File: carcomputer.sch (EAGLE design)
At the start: 23 parts, among them K1 351, Q1 BUZ10, Q2 BUZ10, T1 2N2219, X1 B3B-ZR

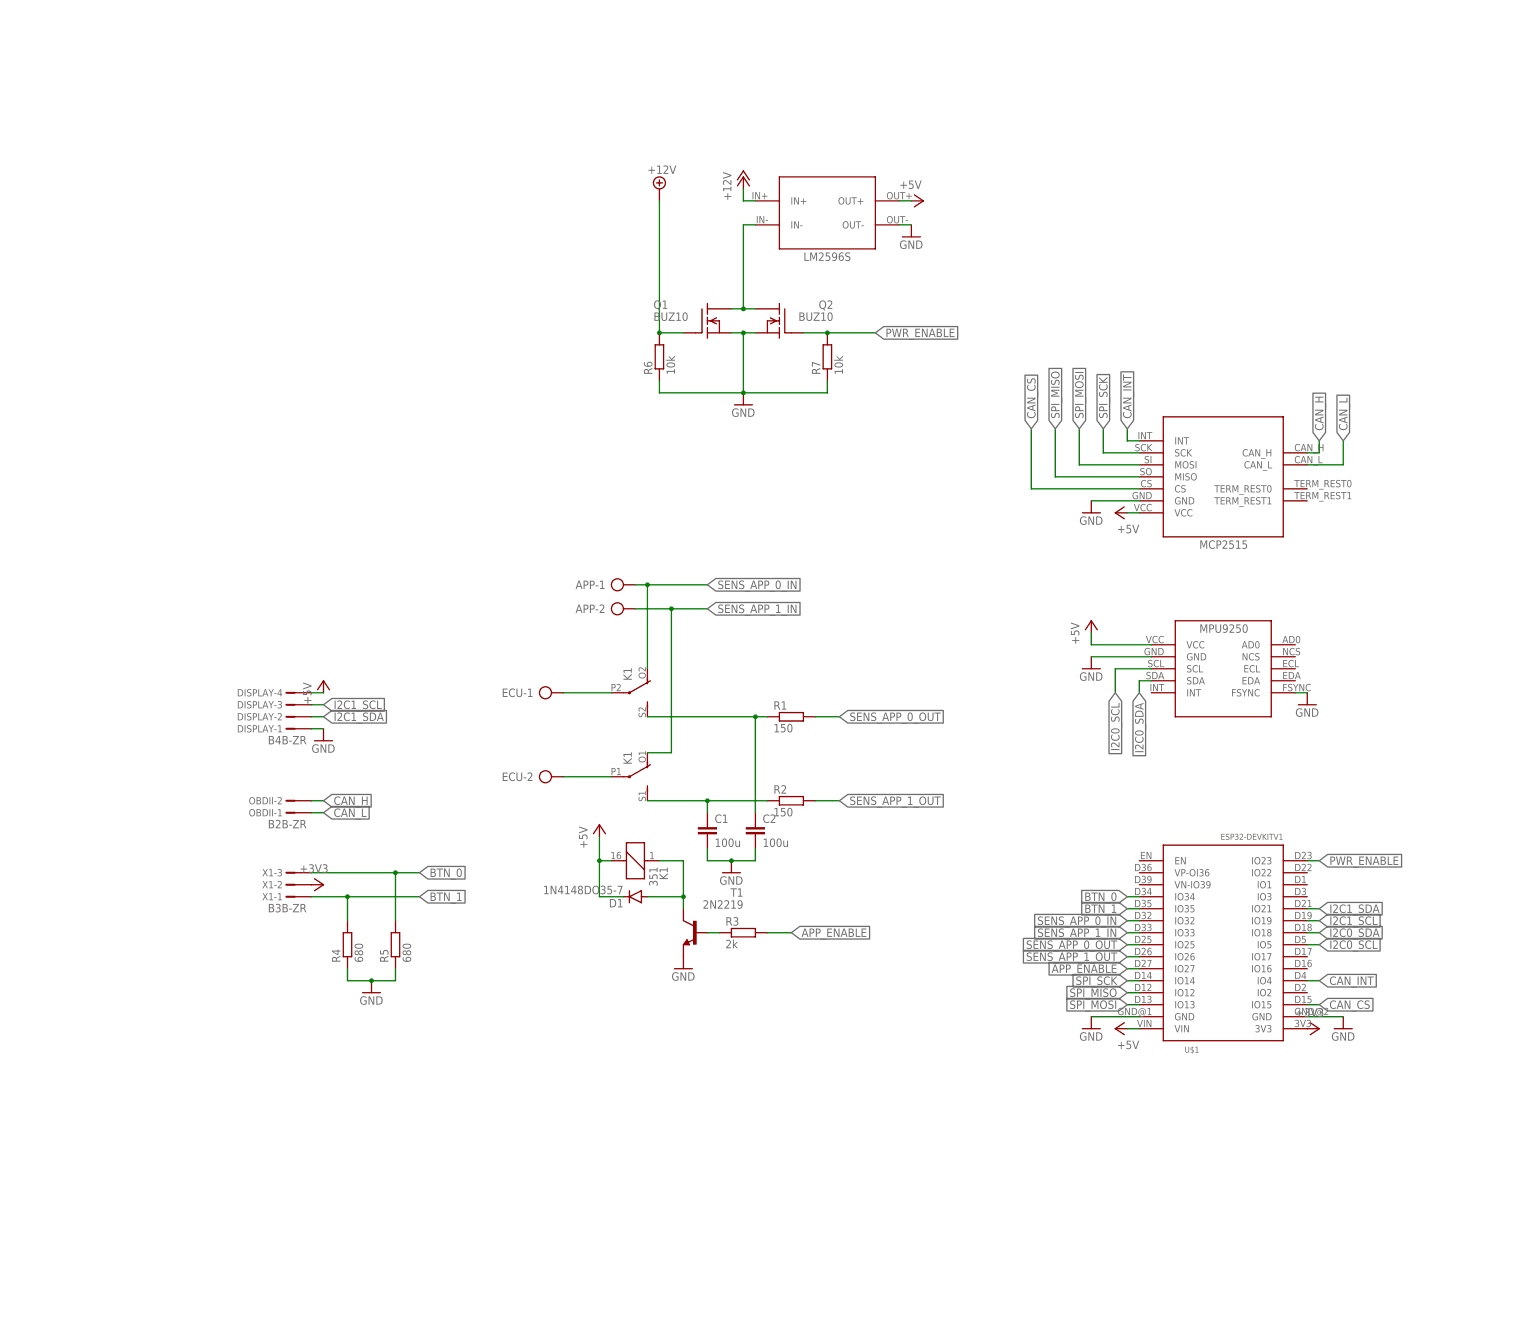
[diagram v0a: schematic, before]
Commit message: Added alternative power circuit. Added connection jumpers. Remapped some pins.
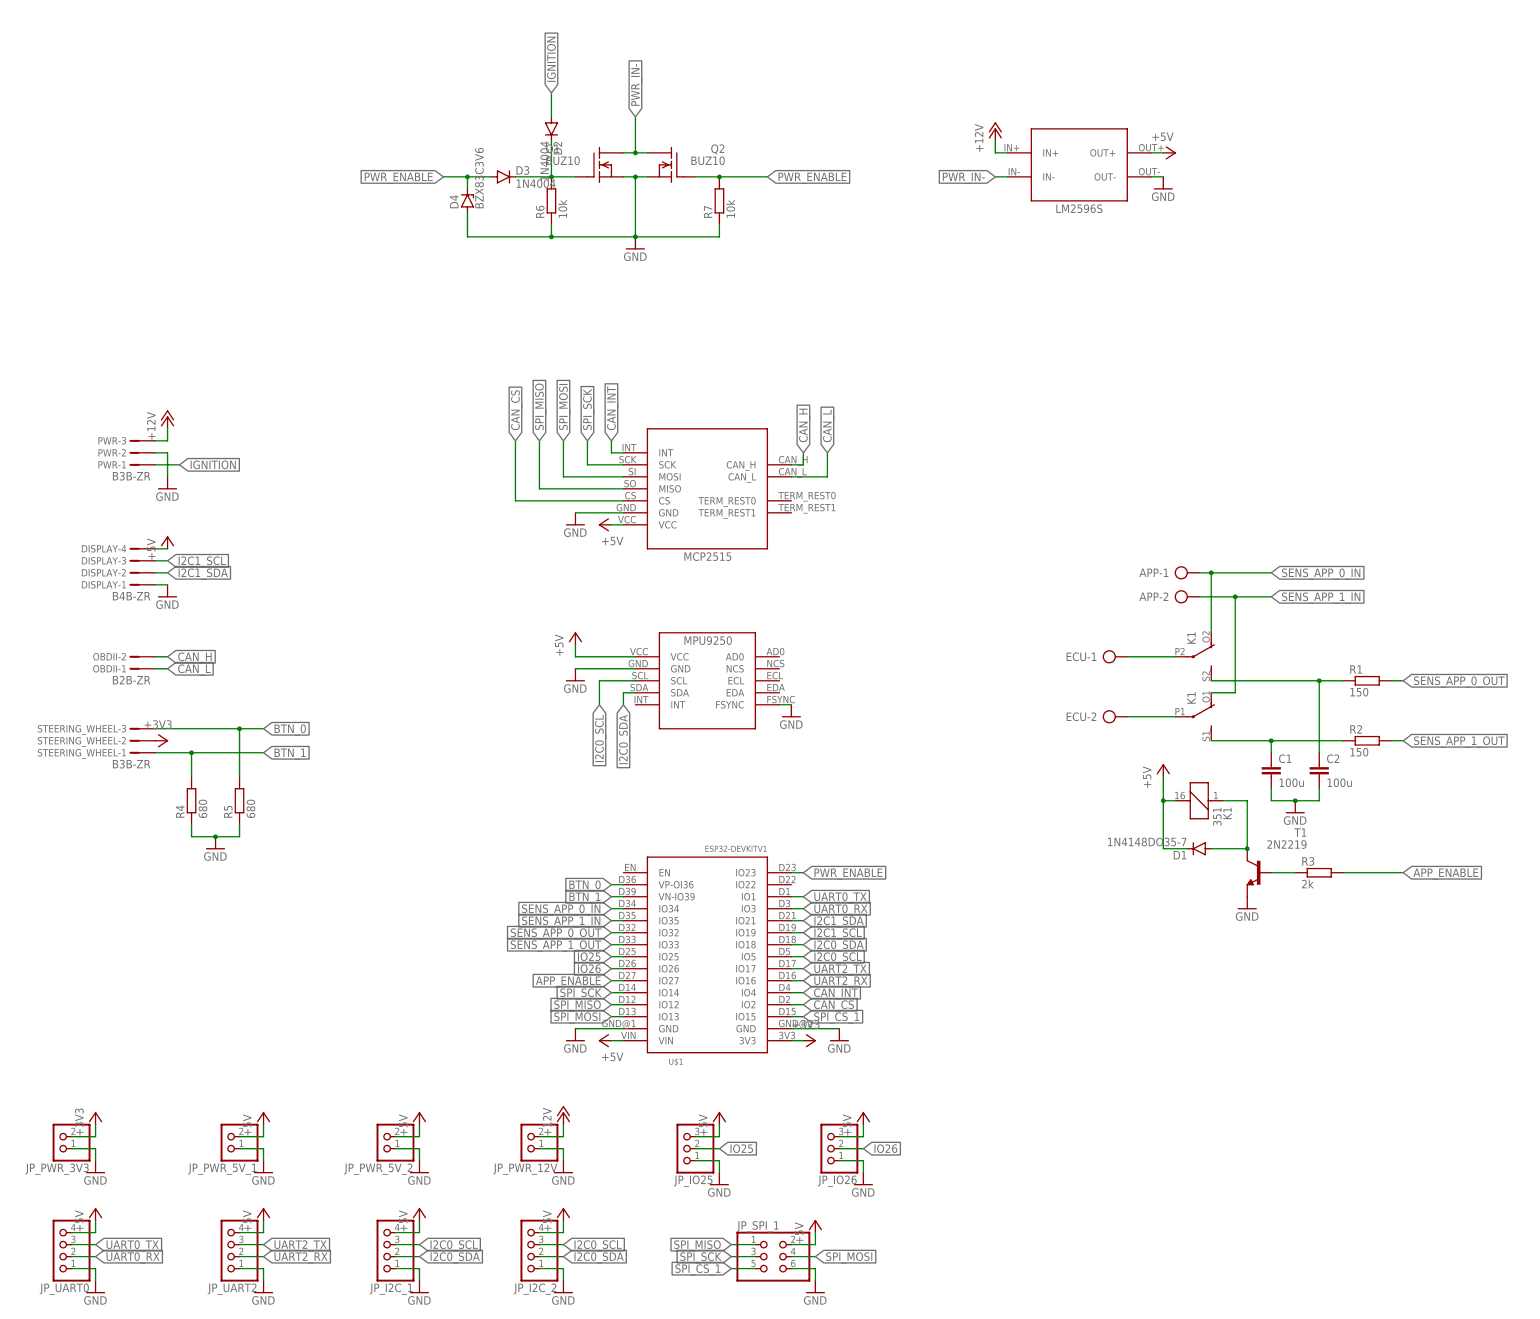
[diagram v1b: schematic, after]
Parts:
- removed X1: B3B-ZR, con-jst-custom:B3B-ZR
- added D2, D3: 1N4004, diode:1N4004
- added D4: BZX83C3V6, diode:BZX85
- added JP_I2C_1, JP_I2C_2, JP_UART0, JP_UART2: (no value), pinhead:PINHD-1X4
- added JP_IO25, JP_IO26: (no value), pinhead:PINHD-1X3
- added JP_PWR_12V, JP_PWR_3V3, JP_PWR_5V_1, JP_PWR_5V_2: (no value), pinhead:PINHD-1X2
- added JP_SPI_1: (no value), pinhead:PINHD-2X3
- added PWR, STEERING_WHEEL: B3B-ZR, con-jst-custom:B3B-ZR
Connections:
- net N$8 renamed PWR_IN-
- new net IGNITION: D2.A, PWR-1.1
- new net IO25: JP_IO25.2, U$1.IO25
- new net IO26: JP_IO26.2, U$1.IO26
- new net N$5: D2.C, D3.C, Q1.G, R6.2
- new net SPI_CS_1: JP_SPI_1.5, U$1.IO15
- new net UART0_RX: JP_UART0.2, U$1.IO3
- new net UART0_TX: JP_UART0.3, U$1.IO1
- new net UART2_RX: JP_UART2.2, U$1.IO16
- new net UART2_TX: JP_UART2.3, U$1.IO17
- net +12V: now also JP_PWR_12V.2, PWR-3.1; no longer Q1.G, R6.2
- net +3V3: now also JP_PWR_3V3.2, STEERING_WHEEL-2.1; no longer X1-2.1
- net +5V: now also JP_I2C_1.4, JP_I2C_2.4, JP_IO25.3, JP_IO26.3, JP_PWR_5V_1.2, JP_PWR_5V_2.2, JP_SPI_1.2, JP_UART0.4, JP_UART2.4
- net BTN_0: now also STEERING_WHEEL-3.1, U$1.VP-OI36; no longer U$1.IO34, X1-3.1
- net BTN_1: now also STEERING_WHEEL-1.1, U$1.VN-IO39; no longer U$1.IO35, X1-1.1
- net CAN_CS: now also U$1.IO2; no longer U$1.IO15
- net GND: now also D4.A, JP_I2C_1.1, JP_I2C_2.1, JP_IO25.1, JP_IO26.1, JP_PWR_12V.1, JP_PWR_3V3.1, JP_PWR_5V_1.1, JP_PWR_5V_2.1, JP_SPI_1.6, JP_UART0.1, JP_UART2.1, PWR-2.1
- net I2C0_SCL: now also JP_I2C_1.3, JP_I2C_2.3
- net I2C0_SDA: now also JP_I2C_1.2, JP_I2C_2.2
- net PWR_ENABLE: now also D3.A, D4.C
- net SENS_APP_0_IN: now also U$1.IO34; no longer U$1.IO32
- net SENS_APP_0_OUT: now also U$1.IO32; no longer U$1.IO25
- net SENS_APP_1_IN: now also U$1.IO35; no longer U$1.IO33
- net SENS_APP_1_OUT: now also U$1.IO33; no longer U$1.IO26
- net SPI_MISO: now also JP_SPI_1.1
- net SPI_MOSI: now also JP_SPI_1.4
- net SPI_SCK: now also JP_SPI_1.3
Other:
- moved on the sheet: APP-1, APP-2, C1, C2, D1, DISPLAY-1, DISPLAY-2, DISPLAY-3, DISPLAY-4, ECU-1, ECU-2, K1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

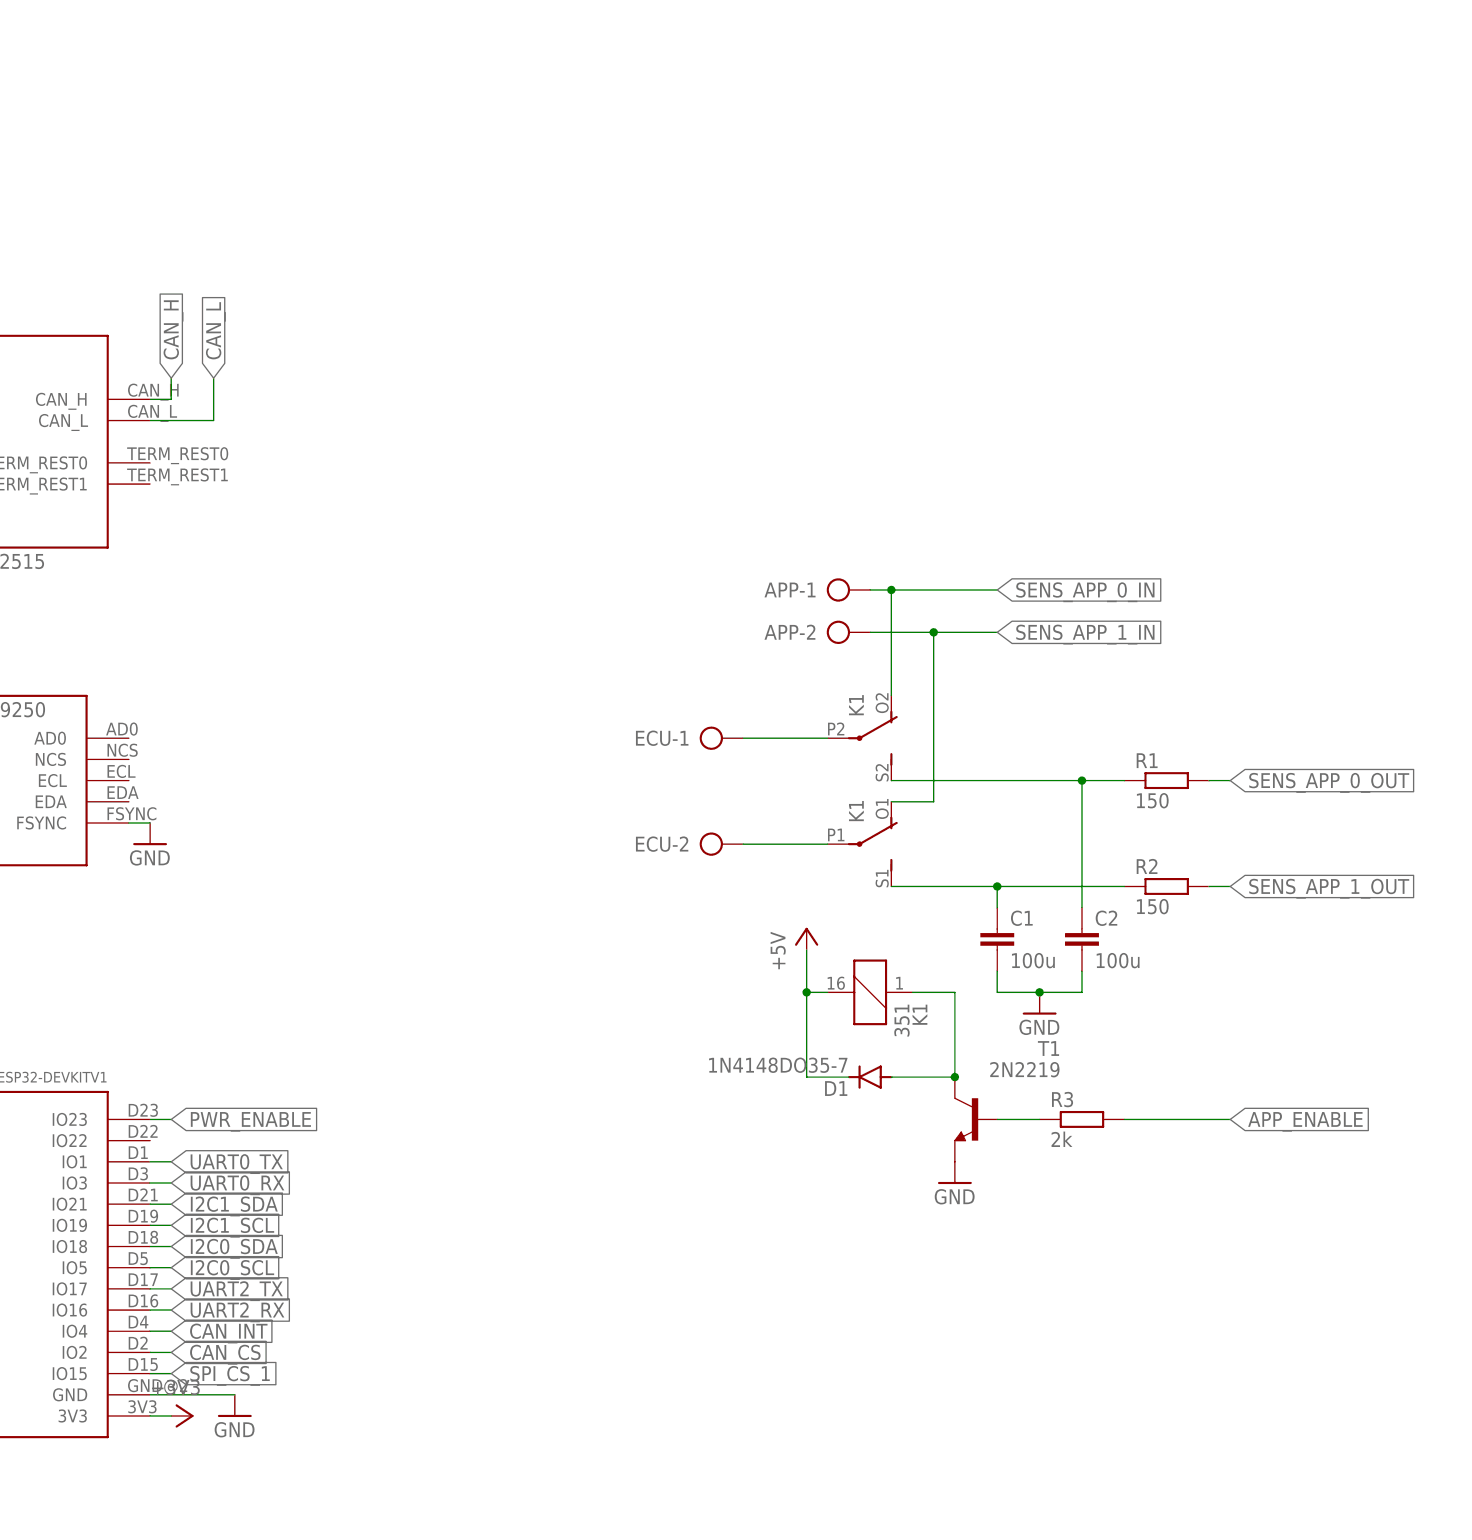
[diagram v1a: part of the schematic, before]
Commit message: Added SD card module (footprint is not accurate)
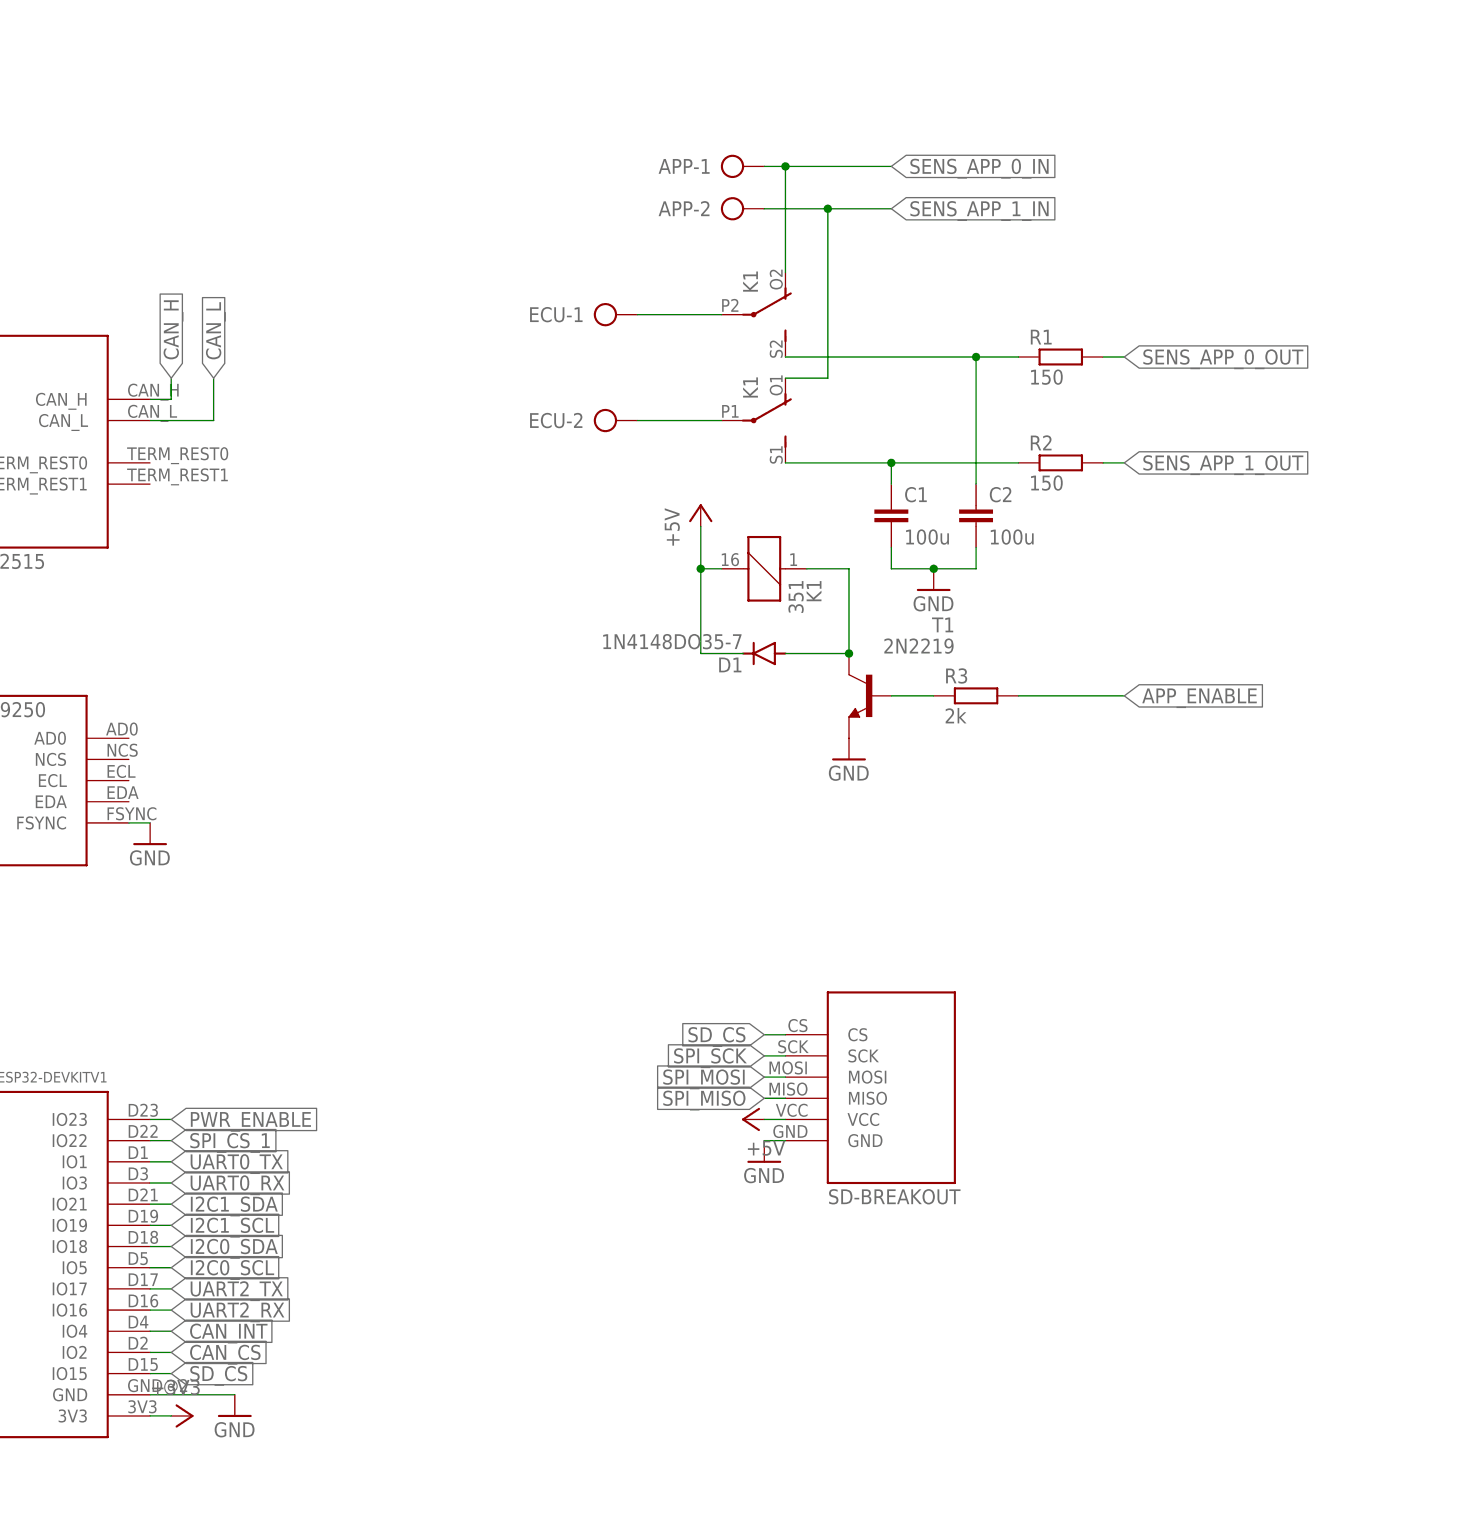
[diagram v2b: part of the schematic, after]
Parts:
- added U$5: HKD-MICRO-SD-BREAKOUT, sd-mmc:HKD-MICRO-SD-BREAKOUT
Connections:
- new net SD_CS: U$1.IO15, U$5.CS
- net +5V: now also U$5.VCC
- net GND: now also U$5.GND
- net SPI_CS_1: now also U$1.IO22; no longer U$1.IO15
- net SPI_MISO: now also U$5.MISO
- net SPI_MOSI: now also U$5.MOSI
- net SPI_SCK: now also U$5.SCK
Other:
- moved on the sheet: APP-1, APP-2, C1, C2, D1, ECU-1, ECU-2, K1, R1, R2, R3, T1
